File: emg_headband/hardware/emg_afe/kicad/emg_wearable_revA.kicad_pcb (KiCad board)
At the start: 2 copper layers, 0 parts

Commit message: EMG Rev A: fit 2.5x1in flex board, start layout
One 3.5 mm jack (CH1) plus the 1 mm FPC for CH1-CH3, isolated UART
dropped, LiPo on solder pads, XIAO soldered by its castellations.
Board outline 63.5 x 25.4 mm with flex design rules and first-pass
placement (XIAO left with USB-C down, ADS1298 middle, jack/FPC right).
Not routed yet.

Co-Authored-By: Claude Opus 5.5 (1M context) <noreply@anthropic.com>
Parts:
- added C101: 1uF, Capacitor_SMD:C_0603_1608Metric, F.Cu at (71.6, 56.0)
- added C102: 100nF, Capacitor_SMD:C_0603_1608Metric, F.Cu at (71.6, 57.7)
- added C107: 10uF, Capacitor_SMD:C_0603_1608Metric, F.Cu at (71.6, 59.4)
- added C111: 1.5nF C0G, Capacitor_SMD:C_0603_1608Metric, F.Cu at (82.4, 73.6)
- added C112: 10uF, Capacitor_SMD:C_0603_1608Metric, F.Cu at (82.4, 51.8)
- added C113: 100nF, Capacitor_SMD:C_0603_1608Metric, F.Cu at (82.4, 54.3)
- added C114: 22uF, Capacitor_SMD:C_0603_1608Metric, F.Cu at (79.2, 51.8)
- added C115: 1uF, Capacitor_SMD:C_0603_1608Metric, F.Cu at (76.0, 54.3)
- added C116: 1uF, Capacitor_SMD:C_0603_1608Metric, F.Cu at (79.2, 73.6)
- added C117: 1uF, Capacitor_SMD:C_0603_1608Metric, F.Cu at (79.2, 54.3)
- added C118: 10uF, Capacitor_SMD:C_0603_1608Metric, F.Cu at (85.6, 51.8)
- added C119: 100nF, Capacitor_SMD:C_0603_1608Metric, F.Cu at (79.2, 71.0)
- added C120: 100nF, Capacitor_SMD:C_0603_1608Metric, F.Cu at (85.6, 54.3)
- added C121: 1uF, Capacitor_SMD:C_0603_1608Metric, F.Cu at (76.0, 73.6)
- added C122: 100nF, Capacitor_SMD:C_0603_1608Metric, F.Cu at (76.0, 71.0)
- added C201: 1nF C0G, Capacitor_SMD:C_0603_1608Metric, F.Cu at (89.6, 56.0)
- added C202: 1nF C0G, Capacitor_SMD:C_0603_1608Metric, F.Cu at (89.6, 57.6)
- added C203: 1nF C0G, Capacitor_SMD:C_0603_1608Metric, F.Cu at (89.6, 59.2)
- added C204: 1nF C0G, Capacitor_SMD:C_0603_1608Metric, F.Cu at (89.6, 60.8)
- added C205: 1nF C0G, Capacitor_SMD:C_0603_1608Metric, F.Cu at (89.6, 62.4)
- added C206: 1nF C0G, Capacitor_SMD:C_0603_1608Metric, F.Cu at (89.6, 64.0)
- added D101: B5819W, Diode_SMD:D_SOD-123, F.Cu at (71.6, 62.0)
- added J1: CH1 (TRS), Connector_Audio:Jack_3.5mm_CUI_SJ-3523-SMT_Horizontal, F.Cu at (105.0, 56.3)
- added J3: LiPo pads (protected cell), emg_wearable:LiPo_SolderPads_2x2.0x3.0mm_P3.5mm, F.Cu at (55.0, 52.2)
- added J6: FLEX ARRAY CH1-3 (FPC 12P 0.5mm, 1mm tall), emg_wearable:Hirose_FH34SRJ-12S-0.5SH_1x12-1MP_P0.50mm_Horizontal, F.Cu at (112.7, 69.5)
- added Q101: AO3401A, Package_TO_SOT_SMD:SOT-23, F.Cu at (71.6, 65.0)
- added R101: 1M, Resistor_SMD:R_0603_1608Metric, F.Cu at (82.4, 71.0)
- added R102: 330k, Resistor_SMD:R_0603_1608Metric, F.Cu at (85.6, 71.0)
- added R103: 10k, Resistor_SMD:R_0603_1608Metric, F.Cu at (71.6, 69.7)
- added R104: 100k, Resistor_SMD:R_0603_1608Metric, F.Cu at (71.6, 68.0)
- added R105: 10k, Resistor_SMD:R_0603_1608Metric, F.Cu at (71.6, 71.4)
- added R106: 10k, Resistor_SMD:R_0603_1608Metric, F.Cu at (71.6, 73.1)
- added R201: 22k, Resistor_SMD:R_0603_1608Metric, F.Cu at (93.0, 56.0)
- added R202: 22k, Resistor_SMD:R_0603_1608Metric, F.Cu at (93.0, 57.6)
- added R203: 22k, Resistor_SMD:R_0603_1608Metric, F.Cu at (93.0, 59.2)
- added R204: 22k, Resistor_SMD:R_0603_1608Metric, F.Cu at (93.0, 60.8)
- added R205: 22k, Resistor_SMD:R_0603_1608Metric, F.Cu at (93.0, 62.4)
- added R206: 22k, Resistor_SMD:R_0603_1608Metric, F.Cu at (93.0, 64.0)
- added TP1: +3V0_A, TestPoint:TestPoint_Pad_D1.0mm, F.Cu at (97.0, 67.0)
- added TP2: +3V3, TestPoint:TestPoint_Pad_D1.0mm, F.Cu at (100.0, 67.0)
- added TP3: AGND, TestPoint:TestPoint_Pad_D1.0mm, F.Cu at (103.0, 67.0)
- added TP4: VSYS, TestPoint:TestPoint_Pad_D1.0mm, F.Cu at (106.0, 67.0)
- added TP5: RLD_OUT, TestPoint:TestPoint_Pad_D1.0mm, F.Cu at (97.0, 71.0)
- added TP6: ADS_DRDY, TestPoint:TestPoint_Pad_D1.0mm, F.Cu at (100.0, 71.0)
- added TP7: SPI_SCK, TestPoint:TestPoint_Pad_D1.0mm, F.Cu at (103.0, 71.0)
- added TP8: AGND, TestPoint:TestPoint_Pad_D1.0mm, F.Cu at (106.0, 71.0)
- added U1: ADS1298IPAGR, Package_QFP:TQFP-64_10x10mm_P0.5mm, F.Cu at (81.0, 62.7)
- added U2: XIAO ESP32-S3, emg_wearable:XIAO_ESP32S3_SMD, F.Cu at (59.4, 64.9)
- added U6: LP5907MFX-3.0, Package_TO_SOT_SMD:SOT-23-5, F.Cu at (71.6, 53.2)
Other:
- board outline added: 63.5 x 25.4 mm

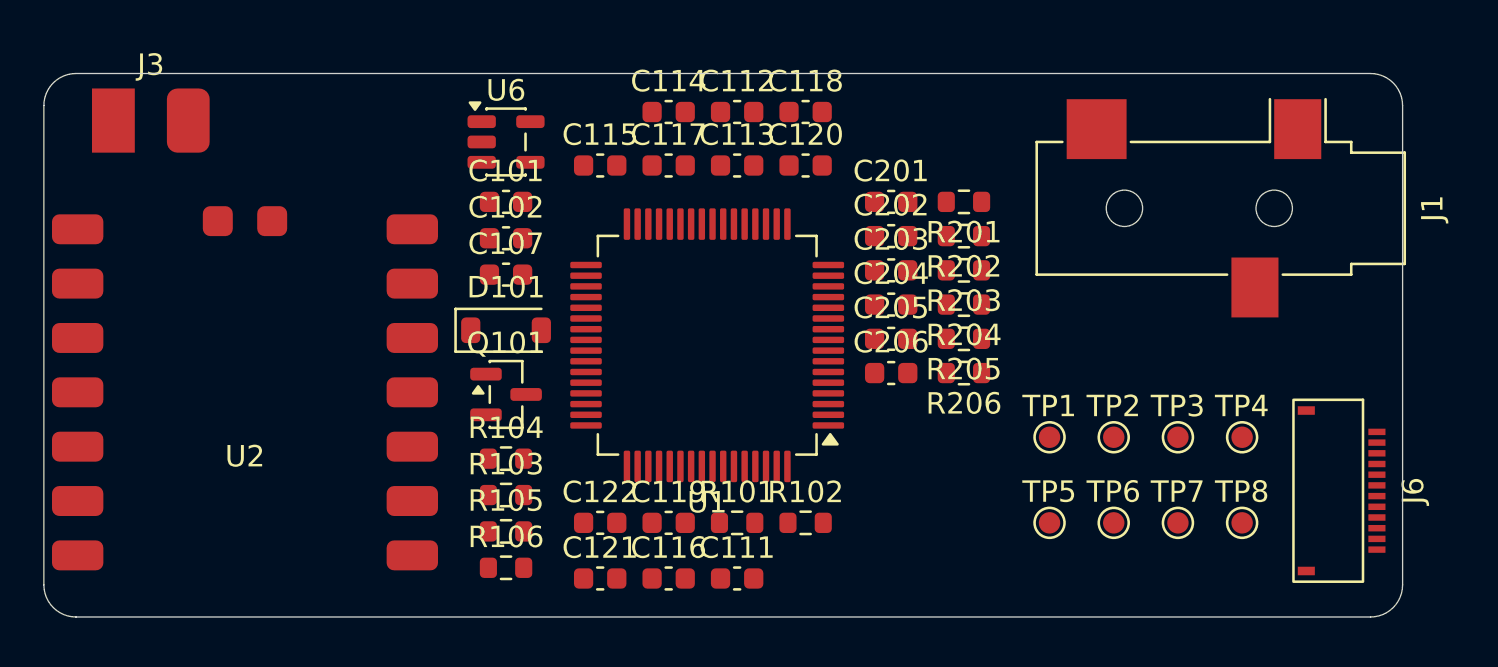
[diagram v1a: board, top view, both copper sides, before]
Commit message: EMG Rev A: route the 2.5x1in flex board and add JLC fab outputs
Freerouting pass plus fixes: FPC pins reordered to match the input RC
column, input filters spaced out, SPI clock moved to XIAO D5, SCLK/DRDY
test points dropped, top-layer keepout under the XIAO. AGND pours on
both layers with stitching vias, silkscreen refs hidden, back-side
labels, stiffener areas on User.1. DRC clean except J1 silk at the
board edge. Gerbers, drill, JLC BOM and CPL in kicad/fab/.

Co-Authored-By: Claude Opus 5.5 (1M context) <noreply@anthropic.com>
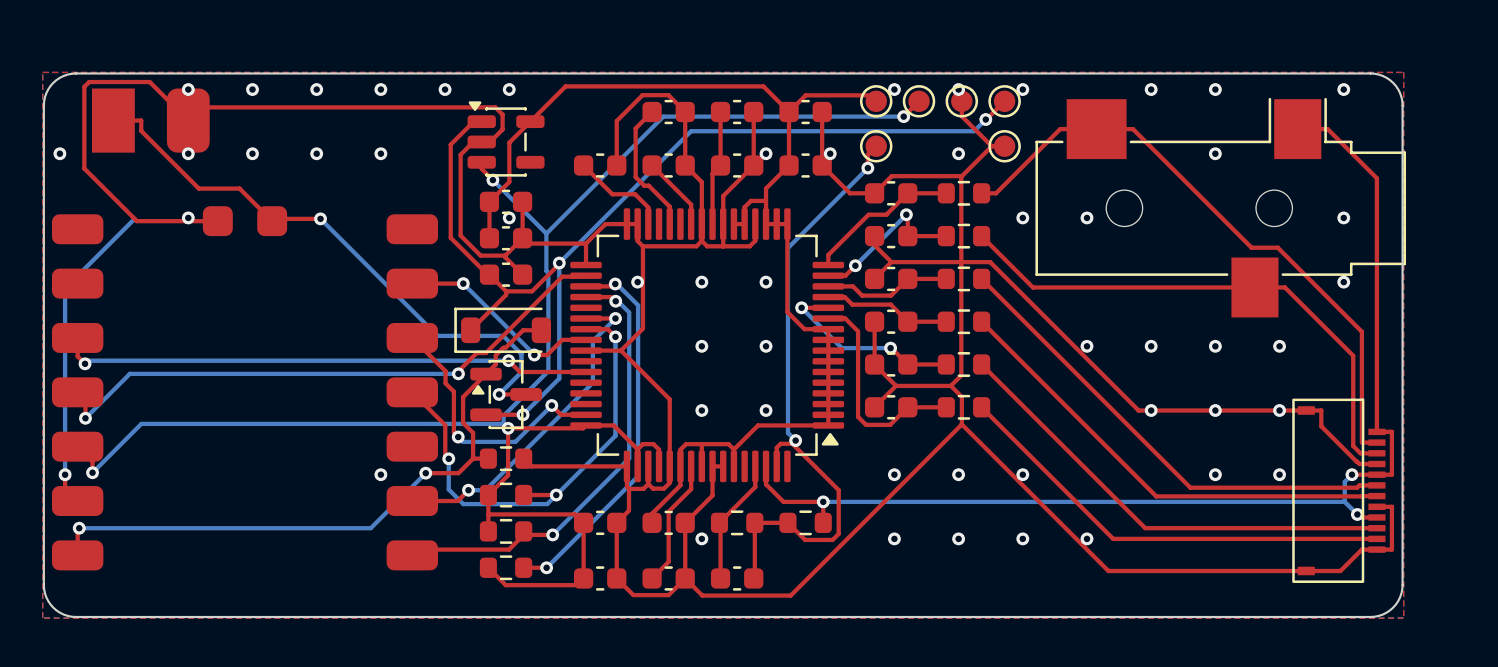
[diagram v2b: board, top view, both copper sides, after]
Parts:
- removed TP6: ADS_DRDY, TestPoint:TestPoint_Pad_D1.0mm
- removed TP7: SPI_SCK, TestPoint:TestPoint_Pad_D1.0mm
- moved TP8 20.8 mm to (94.9, 53.4)
- moved TP5 19.4 mm to (88.9, 53.4)
- moved TP4 19.2 mm to (94.9, 51.3)
- moved TP3 18.7 mm to (92.9, 51.3)
- moved TP2 18.1 mm to (90.9, 51.3)
- moved TP1 17.7 mm to (88.9, 51.3)
- moved C206 1.60 mm to (89.6, 65.6), turned to 180 degrees
- moved R206 1.60 mm to (93.0, 65.6)
- moved C205 1.20 mm to (89.6, 63.6), turned to 180 degrees
- moved R205 1.20 mm to (93.0, 63.6)
- moved C204 0.80 mm to (89.6, 61.6), turned to 180 degrees
- moved R204 0.80 mm to (93.0, 61.6)
- moved C201 0.40 mm to (89.6, 55.6), turned to 180 degrees
- moved C203 0.40 mm to (89.6, 59.6), turned to 180 degrees
- moved R201 0.40 mm to (93.0, 55.6)
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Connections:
- J6 pad 10: ELEC3_P -> ELEC1_N
- J6 pad 11: ELEC3_N -> ELEC1_P
- J6 pad 2: ELEC1_P -> ELEC3_N
- J6 pad 3: ELEC1_N -> ELEC3_P
- J6 pad 6: ELEC2_P -> ELEC2_N
- J6 pad 7: ELEC2_N -> ELEC2_P
- U2 pad 6: (no net) -> SPI_SCK
- U2 pad 9: SPI_SCK -> (no net)
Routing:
- net AGND: track 0.00 -> 238.3 mm, vias 0 -> 53
- net +3V3: track 0.00 -> 83.0 mm, vias 0 -> 4
- net +3V0_A: track 0.00 -> 57.4 mm
- net RLD_ELEC: track 0.00 -> 53.5 mm, vias 0 -> 3
- net VSYS: track 0.00 -> 48.9 mm, vias 0 -> 3
- net VBUS: track 0.00 -> 30.0 mm, vias 0 -> 2
- net RLD_OUT: track 0.00 -> 29.6 mm, vias 0 -> 2
- net ELEC1_P: track 0.00 -> 28.8 mm
- net SPI_MOSI: track 0.00 -> 27.6 mm, vias 0 -> 2
- net VBAT: track 0.00 -> 27.5 mm, vias 0 -> 2
- net ELEC1_N: track 0.00 -> 25.2 mm
- net SPI_MISO: track 0.00 -> 25.0 mm, vias 0 -> 2
- net ELEC2_P: track 0.00 -> 22.6 mm
- net ADS_CS: track 0.00 -> 22.3 mm, vias 0 -> 3
- net ELEC2_N: track 0.00 -> 21.9 mm
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- added copper zone on B.Cu, net AGND
- added copper zone on F.Cu, net AGND
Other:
- board text added: "EMG AFE REV A"
- board text added: "LIPO + -"
- board text added: "STIFFENER: 0.2 mm FR4 on the back, 3 areas. Unstiffened bend zones: x 68.6-74.2 and 88.0-95.8 (gentle bends only)."
- board text added: "USB ON: ELECTRODES OFF OR LAPTOP ON BATTERY"

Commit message: EMG Rev A: shorten flex board to 57 mm, face the FPC outward
J6 rotated so its FPC opening (mounting-tab side) is on the board edge;
FPC pinout back to CH1 at pins 2-4. Input RC filters moved next to J6,
test pads moved to the back under the RC block. Board 57 x 25.4 mm,
re-routed, AGND pours and stitching vias, stiffener outlines updated.
DRC clean except J1 silk at the board edge. Fab outputs regenerated.

Co-Authored-By: Claude Opus 5.5 (1M context) <noreply@anthropic.com>
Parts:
- TP1, TP2, TP3, TP4, TP5, TP8: moved to B.Cu
- moved TP4 21.7 mm to (89.2, 72.2), turned to 180 degrees
- moved TP5 18.9 mm to (91.2, 72.2), turned to 180 degrees
- moved TP8 18.9 mm to (93.2, 72.2), turned to 180 degrees
- moved TP1 18.7 mm to (89.2, 70.0), turned to 180 degrees
- moved TP2 18.7 mm to (91.2, 70.0), turned to 180 degrees
- moved TP3 18.7 mm to (93.2, 70.0), turned to 180 degrees
- moved R206 10.3 mm to (99.5, 73.6)
- moved R201 10.3 mm to (99.5, 63.6)
- moved R203 10.3 mm to (99.5, 67.6)
- moved R204 10.3 mm to (99.5, 69.6)
- moved R205 10.3 mm to (99.5, 71.6)
- moved R202 10.3 mm to (99.5, 65.6)
- moved J6 10.2 mm to (102.5, 69.5), turned to 90 degrees
- moved C206 10.2 mm to (95.9, 73.6)
- moved C201 10.2 mm to (95.9, 63.6)
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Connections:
- J6 pad 10: ELEC1_N -> ELEC3_P
- J6 pad 11: ELEC1_P -> ELEC3_N
- J6 pad 2: ELEC3_N -> ELEC1_P
- J6 pad 3: ELEC3_P -> ELEC1_N
- J6 pad 6: ELEC2_N -> ELEC2_P
- J6 pad 7: ELEC2_P -> ELEC2_N
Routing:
- net ELEC2_P: track 22.6 -> 3.26 mm
- net ELEC2_N: track 21.9 -> 2.64 mm
- net ELEC3_P: track 21.6 -> 2.72 mm
- net AGND: track 238.3 -> 254.2 mm, vias 53 -> 40
- net ELEC3_N: track 21.0 -> 5.20 mm
- net ELEC1_N: track 25.2 -> 9.77 mm
- net RLD_OUT: track 29.6 -> 14.4 mm, vias 2 -> 1
- net SPI_MISO: track 25.0 -> 37.1 mm
- net CH3_N: track 10.3 -> 21.0 mm
- net CH2_N: track 5.99 -> 16.3 mm
- net CH2_P: track 6.01 -> 15.2 mm
- net CH3_P: track 9.11 -> 17.8 mm, vias 2 -> 0
- net VBAT: track 27.5 -> 35.3 mm
- net ELEC1_P: track 28.8 -> 21.8 mm
- net CH1_N: track 7.65 -> 14.6 mm, vias 2 -> 0
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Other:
- board size 63.5 x 25.4 mm -> 57 x 25.4 mm
- board text added: "+"
- board text added: "-"
- board text added: "EMG REV A"
- board text added: "STIFFENER 0.2 mm FR4, back side, 3 areas. Bend zones: power column and input RC block."
- board text removed: "EMG AFE REV A"
- board text removed: "LIPO + -"
- board text removed: "STIFFENER: 0.2 mm FR4 on the back, 3 areas. Unstiffened bend zones: x 68.6-74.2 and 88.0-95.8 (gentle bends only)."
- board text removed: "USB ON: ELECTRODES OFF OR LAPTOP ON BATTERY"

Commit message: EMG Rev A: ESP32-S3-MINI-1 on board instead of the XIAO
Replace the hand-soldered XIAO with an ESP32-S3-MINI-1-N8 (antenna at
the board end, copper kept out), HRO USB-C with CC resistors and
USBLC6 ESD, MCP73831 LiPo charger and AP2112K 3.3 V regulator on VSYS.
ADS1298 SPI on IO12-IO18; EN RC plus EN/BOOT test pads instead of
buttons. Board 62.5 x 25.4 mm, re-placed and re-routed, AGND pours,
stiffener outlines updated. ERC: 0 errors (2 datasheet-expected
warnings). DRC: clean apart from connector/module silk at the edge.
JLC BOM/CPL now cover every part except the LiPo and test pads.

Co-Authored-By: Claude Opus 5.5 (1M context) <noreply@anthropic.com>
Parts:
- added C703: 4.7uF, Capacitor_SMD:C_0603_1608Metric, F.Cu at (77.6, 55.3)
- added C704: 4.7uF, Capacitor_SMD:C_0603_1608Metric, F.Cu at (77.6, 57.0)
- added C705: 1uF, Capacitor_SMD:C_0603_1608Metric, F.Cu at (73.2, 55.3)
- added C706: 10uF, Capacitor_SMD:C_0603_1608Metric, F.Cu at (73.2, 57.0)
- added C707: 100nF, Capacitor_SMD:C_0603_1608Metric, F.Cu at (73.2, 58.7)
- added C708: 1uF, Capacitor_SMD:C_0603_1608Metric, F.Cu at (73.2, 74.5)
- added J7: USB-C, Connector_USB:USB_C_Receptacle_HRO_TYPE-C-31-M-12, F.Cu at (61.0, 71.8)
- added R701: 5.1k, Resistor_SMD:R_0603_1608Metric, F.Cu at (77.6, 72.9)
- added R702: 5.1k, Resistor_SMD:R_0603_1608Metric, F.Cu at (77.6, 74.6)
- added R703: 10k, Resistor_SMD:R_0603_1608Metric, F.Cu at (77.6, 58.7)
- added R704: 10k, Resistor_SMD:R_0603_1608Metric, F.Cu at (73.2, 72.8)
- added TP10: BOOT (IO0), TestPoint:TestPoint_Pad_D1.0mm, B.Cu at (75.4, 69.5)
- added TP9: EN (reset), TestPoint:TestPoint_Pad_D1.0mm, B.Cu at (75.4, 66.5)
- added U7: USBLC6-2SC6, Package_TO_SOT_SMD:SOT-23-6, F.Cu at (68.7, 69.0)
- added U8: MCP73831T-2ACI/OT, Package_TO_SOT_SMD:SOT-23-5, F.Cu at (77.6, 52.3)
- added U9: AP2112K-3.3TRG1, Package_TO_SOT_SMD:SOT-23-5, F.Cu at (73.2, 52.3)
- J3: footprint emg_wearable:LiPo_SolderPads_2x2.0x3.0mm_P3.5mm -> emg_wearable:LiPo_SolderPads_2x1.5x2.5mm_P2.6mm
- U2: value XIAO ESP32-S3 -> ESP32-S3-MINI-1-N8; footprint emg_wearable:XIAO_ESP32S3_SMD -> emg_wearable:ESP32-S3-MINI-1
- moved J3 25.3 mm to (68.8, 73.4)
- moved C107 11.7 mm to (77.6, 69.5)
- moved U6 8.55 mm to (73.2, 61.6)
- moved C101 8.45 mm to (73.2, 64.3)
- moved C102 8.45 mm to (73.2, 66.0)
- moved U2 7.48 mm to (63.1, 58.4), turned to 90 degrees
- moved D101 7.21 mm to (77.6, 66.0), turned to 90 degrees
- moved Q101 6.90 mm to (77.6, 61.6)
- moved R104 6.80 mm to (77.6, 71.2)
- moved TP3 5.60 mm to (98.8, 70.0)
- moved TP8 5.60 mm to (98.8, 72.2)
- moved C111 5.50 mm to (87.9, 73.6)
- moved C112 5.50 mm to (87.9, 51.8)
- moved C113 5.50 mm to (87.9, 54.3)
- moved C114 5.50 mm to (84.7, 51.8)
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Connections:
- U2 pad 1: ADS_RESET -> AGND
- U2 pad 10: SPI_MISO -> (no net)
- U2 pad 11: SPI_MOSI -> (no net)
- U2 pad 12: +3V3 -> (no net)
- U2 pad 13: AGND -> (no net)
- U2 pad 14: VBUS -> (no net)
- U2 pad 15: VBAT -> (no net)
- U2 pad 16: AGND -> SPI_SCK
- U2 pad 2: ADS_START -> AGND
- U2 pad 3: (no net) -> +3V3
- U2 pad 4: ADS_CS -> ESP_BOOT
- U2 pad 5: ADS_DRDY -> (no net)
- U2 pad 6: SPI_SCK -> (no net)
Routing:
- net VBUS: track 28.8 -> 69.0 mm, vias 3 -> 5
- net ESP_EN: track 0.00 -> 38.8 mm, vias 0 -> 2
- net AGND: track 254.2 -> 291.0 mm, vias 40 -> 57
- net USB_DN: track 0.00 -> 29.4 mm, vias 0 -> 2
- net USB_DP: track 0.00 -> 26.4 mm, vias 0 -> 2
- net USB_CC1: track 0.00 -> 20.0 mm, vias 0 -> 2
- net SPI_SCK: track 9.50 -> 28.9 mm, vias 0 -> 2
- net ESP_BOOT: track 0.00 -> 18.6 mm, vias 0 -> 1
- net USB_CC2: track 0.00 -> 18.1 mm, vias 0 -> 2
- net SPI_MISO: track 37.1 -> 21.9 mm
- net SPI_MOSI: track 31.6 -> 16.5 mm
- net +3V0_A: track 56.7 -> 71.1 mm, vias 1 -> 2
- net +3V3: track 78.1 -> 89.4 mm, vias 4 -> 5
- net ADS_START: track 21.5 -> 12.4 mm
- net CHG_PROG: track 0.00 -> 8.88 mm
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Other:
- board size 57 x 25.4 mm -> 62.5 x 25.4 mm

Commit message: EMG Rev A: input caps 1 nF -> 100 pF C0G for dry-electrode CMRR
Co-Authored-By: Claude Opus 5.5 (1M context) <noreply@anthropic.com>
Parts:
- C201, C202, C203, C204, C205, C206: value 1nF C0G -> 100pF C0G
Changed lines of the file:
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@@
 			)
 		)
-		(property "Value" "1nF C0G"
+		(property "Value" "100pF C0G"
 			(at 0 1.43 180)
 			(layer "F.Fab")
@@
 			)
 		)
-		(property "Value" "1nF C0G"
+		(property "Value" "100pF C0G"
 			(at 0 1.43 180)
 			(layer "F.Fab")
@@
 			)
 		)
-		(property "Value" "1nF C0G"
+		(property "Value" "100pF C0G"
 			(at 0 1.43 180)
 			(layer "F.Fab")
@@
 			)
 		)
-		(property "Value" "1nF C0G"
+		(property "Value" "100pF C0G"
 			(at 0 1.43 180)
 			(layer "F.Fab")
@@
 			)
 		)
-		(property "Value" "1nF C0G"
+		(property "Value" "100pF C0G"
 			(at 0 1.43 180)
 			(layer "F.Fab")
@@
 			)
 		)
-		(property "Value" "1nF C0G"
+		(property "Value" "100pF C0G"
 			(at 0 1.43 180)
 			(layer "F.Fab")
